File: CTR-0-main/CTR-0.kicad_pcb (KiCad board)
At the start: 2 copper layers, 21 x 51 mm, 38 parts, among them J1 USB_C_Receptacle_USB2.0_14P, J2 Conn_01x20, J3 Conn_01x20, J4 Conn_01x03, SW1 SW_Push, SW2 SW_Push, U1 RP2040, U2 NCP1117-3.3_SOT223, U3 W25Q128JVS, U4 TVS1400DRV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

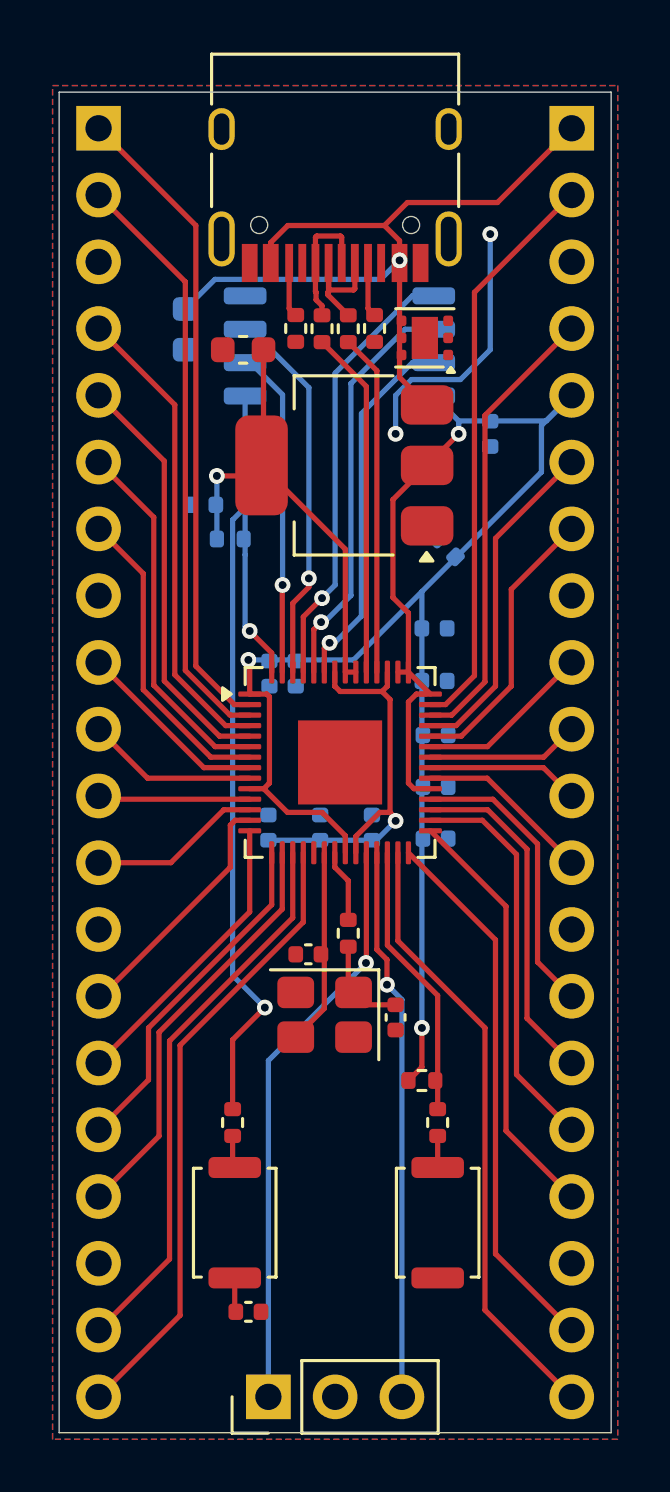
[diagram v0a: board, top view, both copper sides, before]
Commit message: Add files via upload
fixed drc gnd net
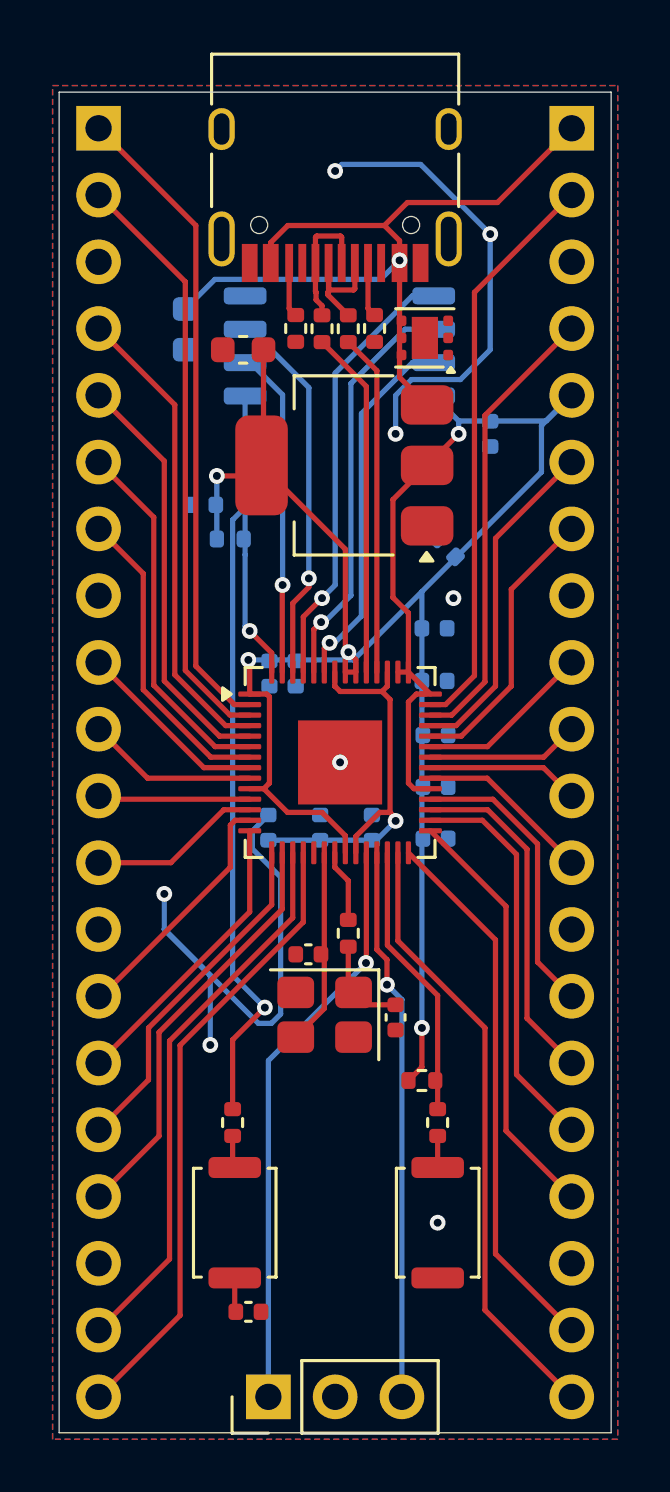
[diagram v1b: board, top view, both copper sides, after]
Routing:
- net GND: track 0.00 -> 38.3 mm, vias 0 -> 8
- net (no net): track 10.4 -> 0.00 mm, vias 2 -> 0
- net +3V3: track 88.6 -> 89.5 mm, vias 4 -> 5
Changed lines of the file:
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@@
+	)
+	(segment
+		(start 188.699 75.074)
+		(end 188.05 75.723)
+		(width 0.2)
+		(layer "F.Cu")
+		(net 1)
+	)
+	(segment
+		(start 188.05 75.723)
+		(end 188.05 76.5)
+		(width 0.2)
+		(layer "F.Cu")
+		(net 1)
+	)
+	(segment
+		(start 192.949998 76.499998)
+		(end 192.95 76.5)
+		(width 0.2)
+		(layer "F.Cu")
+		(net 1)
+	)
+	(segment
+		(start 192.374 75.074)
+		(end 188.699 75.074)
+		(width 0.2)
+		(layer "F.Cu")
+		(net 1)
+	)
+	(segment
+		(start 193.248 74.2)
+		(end 196.675 74.2)
+		(width 0.2)
+		(layer "F.Cu")
+		(net 1)
+	)
+	(segment
+		(start 196.675 74.2)
+		(end 199.5 71.375)
+		(width 0.2)
+		(layer "F.Cu")
+		(net 1)
+	)
+	(segment
+		(start 192.95 80.85)
+		(end 194 81.9)
+		(width 0.2)
+		(layer "F.Cu")
+		(net 1)
+	)
+	(segment
+		(start 192.374 75.074)
+		(end 193.248 74.2)
+		(width 0.2)
+		(layer "F.Cu")
+		(net 1)
+	)
+	(segment
+		(start 192.95 76.5)
+		(end 192.95 75.65)
+		(width 0.2)
+		(layer "F.Cu")
+		(net 1)
+	)
+	(segment
+		(start 192.95 75.65)
+		(end 192.374 75.074)
+		(width 0.2)
+		(layer "F.Cu")
+		(net 1)
+	)
+	(segment
+		(start 192.949998 76.4)
+		(end 192.949998 76.499998)
+		(width 0.2)
+		(layer "F.Cu")
+		(net 1)
+	)
+	(segment
+		(start 192.95 76.5)
+		(end 192.95 80.85)
+		(width 0.2)
+		(layer "F.Cu")
+		(net 1)
+	)
+	(via
+		(at 192.949998 76.4)
+		(size 0.6)
+		(drill 0.3)
+		(layers "F.Cu" "B.Cu")
+		(net 1)
+	)
+	(segment
+		(start 192.225998 77.124)
+		(end 192.949998 76.4)
+		(width 0.2)
+		(layer "B.Cu")
+		(net 1)
+	)
+	(segment
+		(start 184.8 78.25)
+		(end 185.926 77.124)
+		(width 0.2)
+		(layer "B.Cu")
+		(net 1)
+	)
+	(segment
+		(start 185.926 77.124)
+		(end 192.225998 77.124)
+		(width 0.2)
+		(layer "B.Cu")
+		(net 1)
 	)
 	(segment
@@
 		(width 0.2)
 		(layer "F.Cu")
-		(net 0)
+		(net 2)
+	)
+	(via
+		(at 184 100.5)
+		(size 0.6)
+		(drill 0.3)
+		(layers "F.Cu" "B.Cu")
+		(free yes)
+		(net 2)
+	)
+	(via
+		(at 194.4 113.01)
+		(size 0.6)
+		(drill 0.3)
+		(layers "F.Cu" "B.Cu")
+		(free yes)
+		(net 2)
+	)
+	(via
+		(at 185.75 106.25)
+		(size 0.6)
+		(drill 0.3)
+		(layers "F.Cu" "B.Cu")
+		(free yes)
+		(net 2)
+	)
+	(via
+		(at 190.5 73)
+		(size 0.6)
+		(drill 0.3)
+		(layers "F.Cu" "B.Cu")
+		(free yes)
+		(net 2)
+	)
+	(via
+		(at 195 89.25)
+		(size 0.6)
+		(drill 0.3)
+		(layers "F.Cu" "B.Cu")
+		(free yes)
+		(net 2)
+	)
+	(via
+		(at 190.6875 95.5)
+		(size 0.6)
+		(drill 0.3)
+		(layers "F.Cu" "B.Cu")
+		(net 2)
 	)
 	(via
@@
 		(drill 0.3)
 		(layers "F.Cu" "B.Cu")
-		(net 0)
+		(net 2)
 	)
 	(via
@@
 		(drill 0.3)
 		(layers "F.Cu" "B.Cu")
-		(net 0)
+		(net 2)
+	)
+	(segment
+		(start 187.349 98.78655)
+		(end 187.349 98.111)
+		(width 0.2)
+		(layer "B.Cu")
+		(net 2)
+	)
+	(segment
+		(start 187.576363 105.426306)
+		(end 188.074249 105.426306)
+		(width 0.2)
+		(layer "B.Cu")
+		(net 2)
 	)
 	(segment
@@
 		(width 0.2)
 		(layer "B.Cu")
-		(net 0)
+		(net 2)
 	)
 	(segment
@@
 		(width 0.2)
 		(layer "B.Cu")
-		(net 0)
+		(net 2)
+	)
+	(segment
+		(start 184 101.849943)
+		(end 185.75 103.599943)
+		(width 0.2)
+		(layer "B.Cu")
+		(net 2)
+	)
+	(segment
+		(start 184 101.849943)
+		(end 187.576363 105.426306)
+		(width 0.2)
+		(layer "B.Cu")
+		(net 2)
+	)
+	(segment
+		(start 188.074249 105.426306)
+		(end 188.426306 105.074249)
+		(width 0.2)
+		(layer "B.Cu")
+		(net 2)
+	)
+	(segment
+		(start 190.75 72.75)
+		(end 190.5 73)
+		(width 0.2)
+		(layer "B.Cu")
+		(net 2)
 	)
 	(segment
@@
 		(width 0.2)
 		(layer "B.Cu")
-		(net 0)
+		(net 2)
 	)
 	(segment
@@
 		(width 0.2)
 		(layer "B.Cu")
-		(net 0)
+		(net 2)
+	)
+	(segment
+		(start 196.4 75.4)
+		(end 193.75 72.75)
+		(width 0.2)
+		(layer "B.Cu")
+		(net 2)
+	)
+	(segment
+		(start 184 100.5)
+		(end 184 101.849943)
+		(width 0.2)
+		(layer "B.Cu")
+		(net 2)
+	)
+	(segment
+		(start 187.349 98.111)
+		(end 187.96 97.5)
+		(width 0.2)
+		(layer "B.Cu")
+		(net 2)
 	)
 	(segment
@@
 		(width 0.2)
 		(layer "B.Cu")
-		(net 0)
-	)
-	(segment
-		(start 188.699 75.074)
-		(end 188.05 75.723)
-		(width 0.2)
-		(layer "F.Cu")
-		(net 1)
-	)
-	(segment
-		(start 188.05 75.723)
-		(end 188.05 76.5)
-		(width 0.2)
-		(layer "F.Cu")
-		(net 1)
-	)
-	(segment
-		(start 192.949998 76.499998)
-		(end 192.95 76.5)
-		(width 0.2)
-		(layer "F.Cu")
-		(net 1)
-	)
-	(segment
-		(start 192.374 75.074)
-		(end 188.699 75.074)
-		(width 0.2)
-		(layer "F.Cu")
-		(net 1)
-	)
-	(segment
-		(start 193.248 74.2)
-		(end 196.675 74.2)
-		(width 0.2)
-		(layer "F.Cu")
-		(net 1)
-	)
-	(segment
-		(start 196.675 74.2)
-		(end 199.5 71.375)
-		(width 0.2)
-		(layer "F.Cu")
-		(net 1)
-	)
-	(segment
-		(start 192.95 80.85)
-		(end 194 81.9)
-		(width 0.2)
-		(layer "F.Cu")
-		(net 1)
-	)
-	(segment
-		(start 192.374 75.074)
-		(end 193.248 74.2)
-		(width 0.2)
-		(layer "F.Cu")
-		(net 1)
-	)
-	(segment
-		(start 192.95 76.5)
-		(end 192.95 75.65)
-		(width 0.2)
-		(layer "F.Cu")
-		(net 1)
-	)
-	(segment
-		(start 192.95 75.65)
-		(end 192.374 75.074)
-		(width 0.2)
-		(layer "F.Cu")
-		(net 1)
-	)
-	(segment
-		(start 192.949998 76.4)
-		(end 192.949998 76.499998)
-		(width 0.2)
-		(layer "F.Cu")
-		(net 1)
-	)
-	(segment
-		(start 192.95 76.5)
-		(end 192.95 80.85)
-		(width 0.2)
-		(layer "F.Cu")
-		(net 1)
-	)
-	(via
-		(at 192.949998 76.4)
-		(size 0.6)
-		(drill 0.3)
-		(layers "F.Cu" "B.Cu")
-		(net 1)
-	)
-	(segment
-		(start 192.225998 77.124)
-		(end 192.949998 76.4)
-		(width 0.2)
-		(layer "B.Cu")
-		(net 1)
-	)
-	(segment
-		(start 184.8 78.25)
-		(end 185.926 77.124)
-		(width 0.2)
-		(layer "B.Cu")
-		(net 1)
-	)
-	(segment
-		(start 185.926 77.124)
-		(end 192.225998 77.124)
-		(width 0.2)
-		(layer "B.Cu")
-		(net 1)
+		(net 2)
+	)
+	(segment
+		(start 193.75 72.75)
+		(end 190.75 72.75)
+		(width 0.2)
+		(layer "B.Cu")
+		(net 2)
+	)
+	(segment
+		(start 188.426306 99.863856)
+		(end 187.349 98.78655)
+		(width 0.2)
+		(layer "B.Cu")
+		(net 2)
+	)
+	(segment
+		(start 188.426306 105.074249)
+		(end 188.426306 99.863856)
+		(width 0.2)
+		(layer "B.Cu")
+		(net 2)
+	)
+	(segment
+		(start 185.75 103.599943)
+		(end 185.75 106.25)
+		(width 0.2)
+		(layer "B.Cu")
+		(net 2)
+	)
+	(segment
+		(start 191.2875 91.591992)
+		(end 191.003123 91.307615)
+		(width 0.2)
+		(layer "F.Cu")
+		(net 3)
 	)
 	(segment
@@
 	)
 	(segment
+		(start 191.2875 92.0625)
+		(end 191.2875 91.591992)
+		(width 0.2)
+		(layer "F.Cu")
+		(net 3)
+	)
+	(segment
 		(start 193.5 96.5)
 		(end 193.2875 96.2875)
@@
 		(net 3)
 	)
+	(via
+		(at 191.003123 91.307615)
+		(size 0.6)
+		(drill 0.3)
+		(layers "F.Cu" "B.Cu")
+		(net 3)
+	)
